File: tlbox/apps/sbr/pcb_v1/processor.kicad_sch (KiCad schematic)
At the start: 1 part, among them U1 STM32F051R8Tx

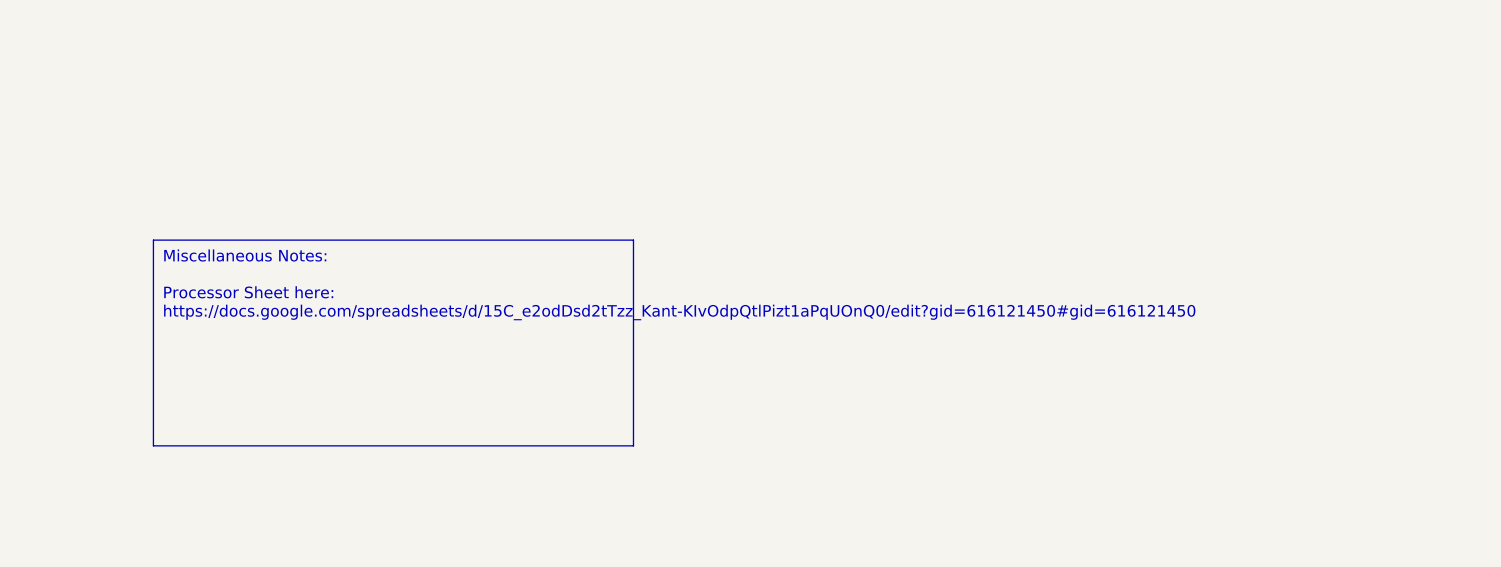
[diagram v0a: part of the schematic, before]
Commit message: update kicad v10
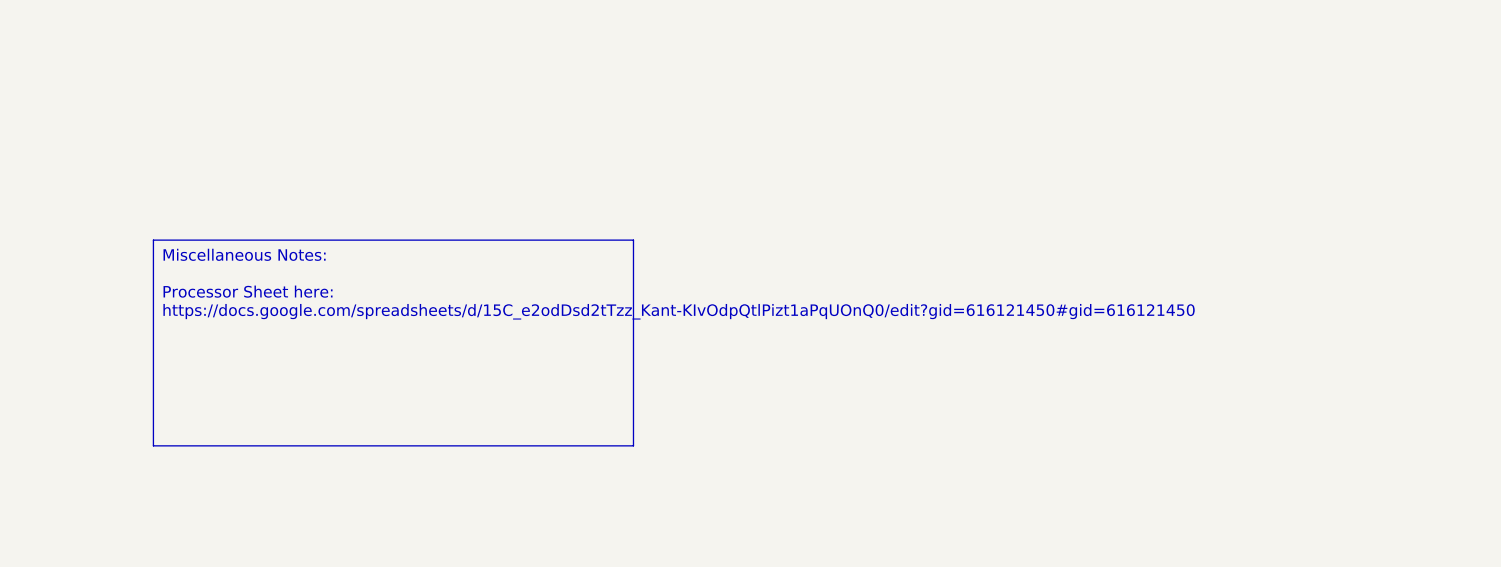
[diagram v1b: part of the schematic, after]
